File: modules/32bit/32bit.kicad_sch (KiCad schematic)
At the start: 53 parts, among them J5 USB_C_Receptacle_USB2.0_14P, SW1 K2-1808SN-A4SW-01, SW2 K2-1808SN-A4SW-01, SW4 K2-1808SN-A4SW-01, U1 ESP32-S3-WROOM-1U-N16R8, U3 MCP6002-xSN

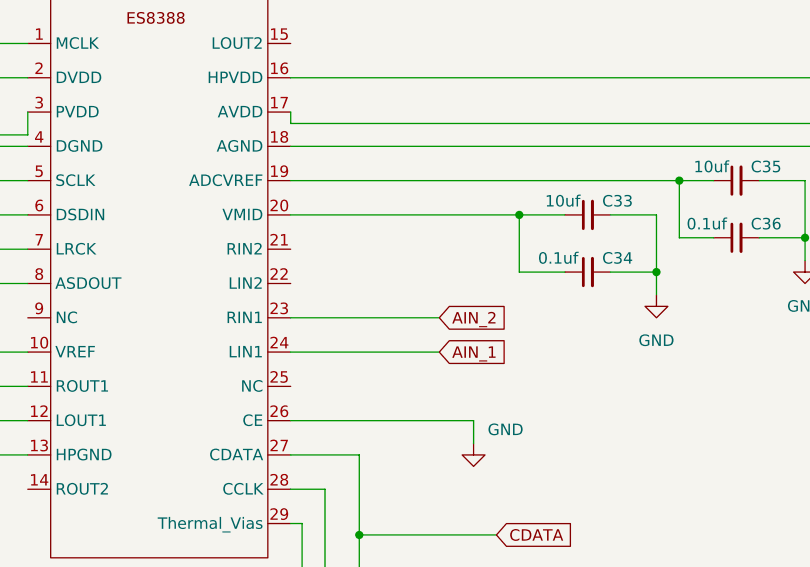
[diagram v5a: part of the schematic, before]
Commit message: Add better routing for power
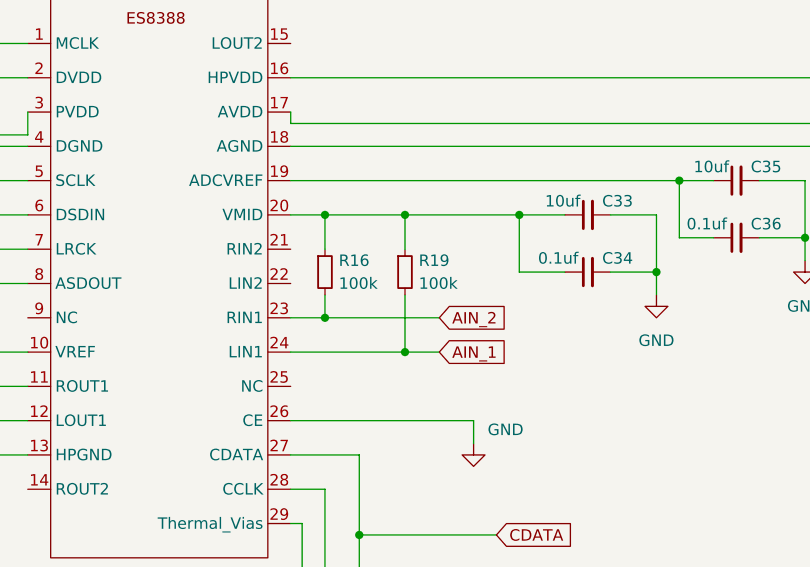
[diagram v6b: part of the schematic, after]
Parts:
- added R16, R19: 100k, Resistor_SMD:R_0402_1005Metric, symbol Device:R_Small
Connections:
- net AIN_1: now also R19.2
- net AIN_2: now also R16.2
- net at C33.1, C34.1, U4.20 (VMID): now also R16.1, R19.1
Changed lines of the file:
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@@
 	)
 	(junction
+		(at 139.7 210.82)
+		(diameter 0)
+		(color 0 0 0 0)
+	)
+	(junction
 		(at 509.27 38.1)
 		(diameter 0)
@@
 	)
 	(junction
+		(at 139.7 226.06)
+		(diameter 0)
+		(color 0 0 0 0)
+	)
+	(junction
 		(at 180.34 95.25)
 		(diameter 0)
@@
 	)
 	(junction
+		(at 130.81 210.82)
+		(diameter 0)
+		(color 0 0 0 0)
+	)
+	(junction
 		(at 45.72 83.82)
 		(diameter 0)
@@
 	)
 	(junction
+		(at 130.81 222.25)
+		(diameter 0)
+		(color 0 0 0 0)
+	)
+	(junction
 		(at 195.58 60.96)
 		(diameter 0)
@@
 	(wire
 		(pts
-			(xy 152.4 210.82) (xy 127 210.82)
+			(xy 152.4 210.82) (xy 139.7 210.82)
 		)
 		(stroke
@@
 	(wire
 		(pts
+			(xy 139.7 226.06) (xy 143.51 226.06)
+		)
+		(stroke
+			(width 0)
+			(type default)
+		)
+	)
+	(wire
+		(pts
 			(xy 45.72 233.68) (xy 53.34 233.68)
 		)
@@
 	(wire
 		(pts
-			(xy 127 222.25) (xy 143.51 222.25)
+			(xy 127 222.25) (xy 130.81 222.25)
 		)
 		(stroke
@@
 	(wire
 		(pts
+			(xy 130.81 222.25) (xy 143.51 222.25)
+		)
+		(stroke
+			(width 0)
+			(type default)
+		)
+	)
+	(wire
+		(pts
 			(xy 130.81 241.3) (xy 127 241.3)
 		)
@@
 	(wire
 		(pts
+			(xy 130.81 219.71) (xy 130.81 222.25)
+		)
+		(stroke
+			(width 0)
+			(type default)
+		)
+	)
+	(wire
+		(pts
 			(xy 127 195.58) (xy 248.92 195.58)
 		)
@@
 	(wire
 		(pts
+			(xy 130.81 210.82) (xy 130.81 214.63)
+		)
+		(stroke
+			(width 0)
+			(type default)
+		)
+	)
+	(wire
+		(pts
 			(xy 63.5 201.93) (xy 97.79 201.93)
 		)
@@
 	(wire
 		(pts
+			(xy 139.7 210.82) (xy 130.81 210.82)
+		)
+		(stroke
+			(width 0)
+			(type default)
+		)
+	)
+	(wire
+		(pts
 			(xy 127 203.2) (xy 203.2 203.2)
 		)
@@
 	(wire
 		(pts
+			(xy 139.7 210.82) (xy 139.7 214.63)
+		)
+		(stroke
+			(width 0)
+			(type default)
+		)
+	)
+	(wire
+		(pts
 			(xy 142.24 251.46) (xy 149.86 251.46)
 		)
@@
 	(wire
 		(pts
+			(xy 139.7 219.71) (xy 139.7 226.06)
+		)
+		(stroke
+			(width 0)
+			(type default)
+		)
+	)
+	(wire
+		(pts
 			(xy 30.48 107.95) (xy 30.48 110.49)
 		)
@@
 	(wire
 		(pts
-			(xy 127 226.06) (xy 143.51 226.06)
+			(xy 127 226.06) (xy 139.7 226.06)
 		)
 		(stroke
@@
 	(wire
 		(pts
+			(xy 130.81 210.82) (xy 127 210.82)
+		)
+		(stroke
+			(width 0)
+			(type default)
+		)
+	)
+	(wire
+		(pts
 			(xy 203.2 222.25) (xy 217.17 222.25)
 		)
@@
 					(unit 1)
 				)
+			)
+		)
+	)
+	(symbol
+		(lib_id "Device:R_Small")
+		(at 130.81 217.17 0)
+		(unit 1)
+		(exclude_from_sim no)
+		(in_bom yes)
+		(on_board yes)
+		(dnp no)
+		(property "Reference" "R16"
+			(at 132.334 215.9 0)
+			(effects
+				(font
+					(size 1.27 1.27)
+				)
+				(justify left)
+			)
+		)
+		(property "Value" "100k"
+			(at 132.334 218.44 0)
+			(effects
+				(font
+					(size 1.27 1.27)
+				)
+				(justify left)
+			)
+		)
+		(property "Footprint" "Resistor_SMD:R_0402_1005Metric"
+			(at 130.81 217.17 0)
+			(effects
+				(font
+					(size 1.27 1.27)
+				)
+				(hide yes)
+			)
+		)
+		(property "Datasheet" "~"
+			(at 130.81 217.17 0)
+			(effects
+				(font
+					(size 1.27 1.27)
+				)
+				(hide yes)
+			)
+		)
+		(property "Description" "Resistor, small symbol"
+			(at 130.81 217.17 0)
+			(effects
+				(font
+					(size 1.27 1.27)
+				)
+				(hide yes)
+			)
+		)
+		(pin "2"
+		)
+		(pin "1"
+		)
+		(instances
+			(project "32bit"
+				(path "/b63493d3-5f6d-47e3-845b-87e7090fc1ab"
+					(reference "R16")
+					(unit 1)
+				)
+			)
+		)
+	)
+	(symbol
+		(lib_id "Device:R_Small")
+		(at 139.7 217.17 0)
+		(unit 1)
+		(exclude_from_sim no)
+		(in_bom yes)
+		(on_board yes)
+		(dnp no)
+		(property "Reference" "R19"
+			(at 141.224 215.9 0)
+			(effects
+				(font
+					(size 1.27 1.27)
+				)
+				(justify left)
+			)
+		)
+		(property "Value" "100k"
+			(at 141.224 218.44 0)
+			(effects
+				(font
+					(size 1.27 1.27)
+				)
+				(justify left)
+			)
+		)
+		(property "Footprint" "Resistor_SMD:R_0402_1005Metric"
+			(at 139.7 217.17 0)
+			(effects
+				(font
+					(size 1.27 1.27)
+				)
+				(hide yes)
+			)
+		)
+		(property "Datasheet" "~"
+			(at 139.7 217.17 0)
+			(effects
+				(font
+					(size 1.27 1.27)
+				)
+				(hide yes)
+			)
+		)
+		(property "Description" "Resistor, small symbol"
+			(at 139.7 217.17 0)
+			(effects
+				(font
+					(size 1.27 1.27)
+				)
+				(hide yes)
+			)
+		)
+		(pin "2"
+		)
+		(pin "1"
+		)
+		(instances
+			(project "32bit"
+				(path "/b63493d3-5f6d-47e3-845b-87e7090fc1ab"
+					(reference "R19")
+					(unit 1)
+				)

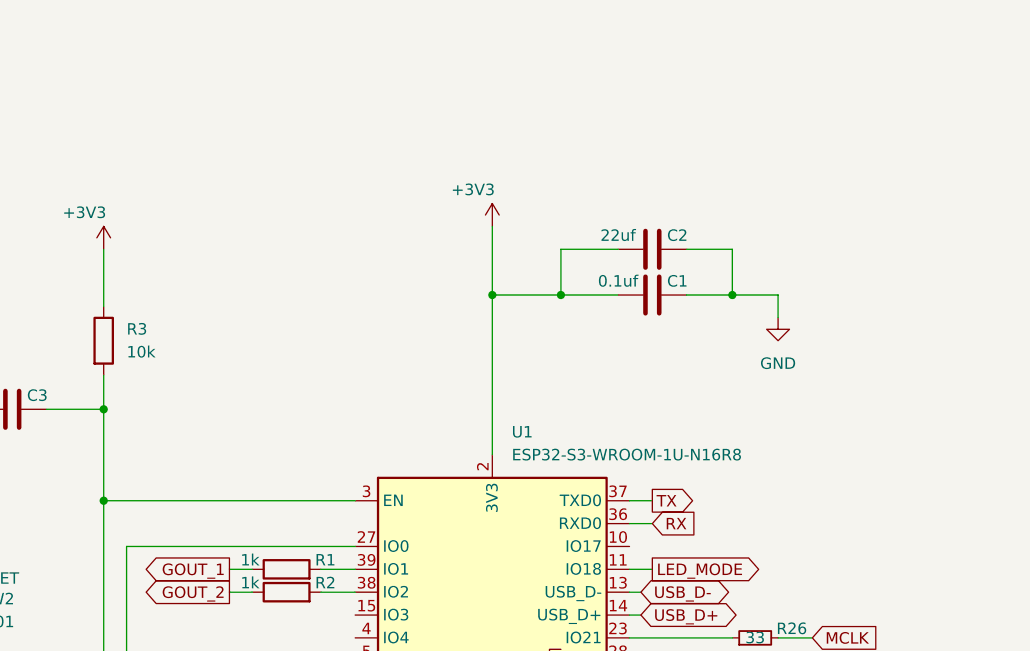
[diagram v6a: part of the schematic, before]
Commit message: Improve 32bit power supply
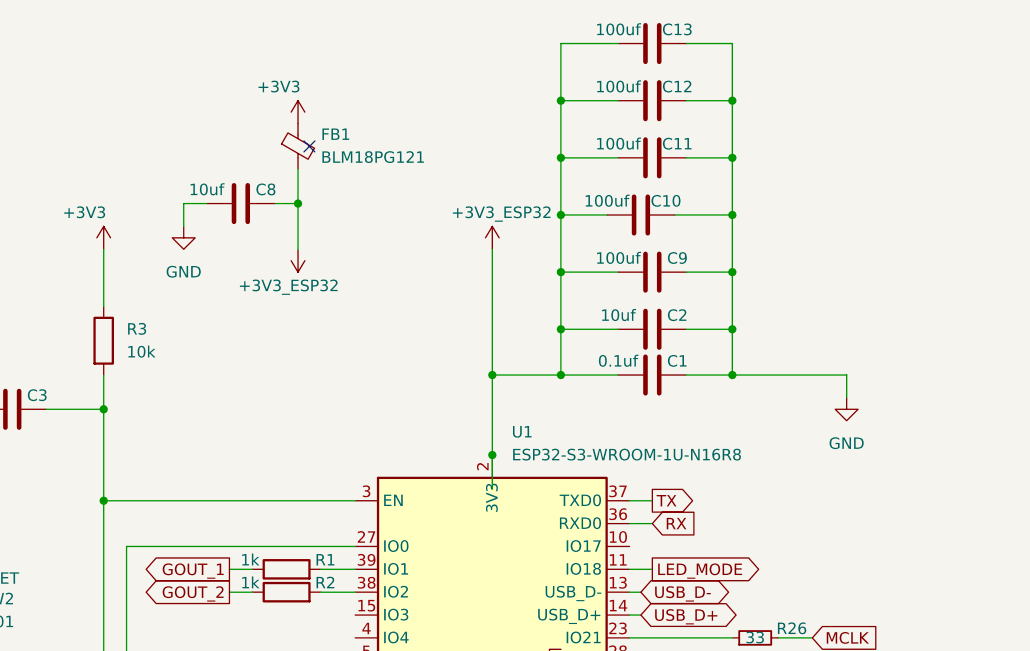
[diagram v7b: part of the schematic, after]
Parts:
- added C10, C11, C12, C13, C9: 100uf, Capacitor_SMD:C_1206_3216Metric, symbol Device:C
- added C8: 10uf, Capacitor_SMD:C_0603_1608Metric, symbol Device:C
- added FB1: BLM18PG121, Capacitor_SMD:C_0201_0603Metric, symbol Device:FerriteBead_Small
- C2: value 22uf -> 10uf
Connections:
- net +3V3: now also FB1.1; no longer C1.1, C2.1, U1.2 (3V3)
- net GND: now also C10.2, C11.2, C12.2, C13.2, C8.1, C9.2
- new net +3V3_ESP32: C1.1, C10.1, C11.1, C12.1, C13.1, C2.1, C8.2, C9.1, FB1.2, U1.2 (3V3)
- no-connect marks 0 -> 1
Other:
- moved on the sheet: C1, C2

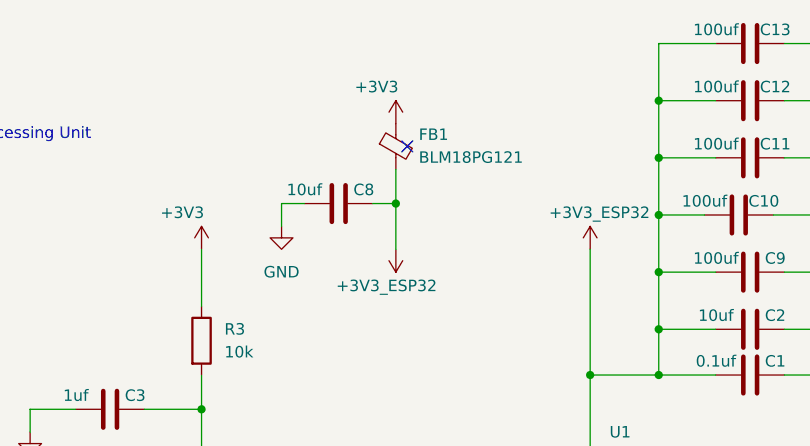
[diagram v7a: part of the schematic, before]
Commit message: 32bit: Use a known ferrite bead
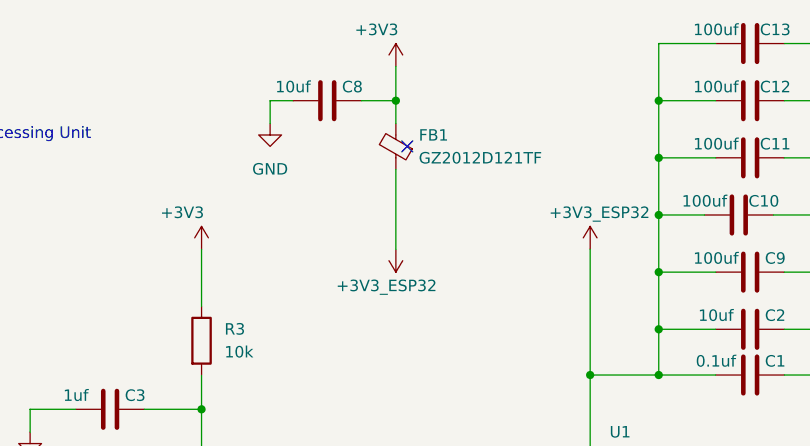
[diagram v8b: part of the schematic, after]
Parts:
- FB1: value BLM18PG121 -> GZ2012D121TF; footprint Capacitor_SMD:C_0201_0603Metric -> Capacitor_SMD:C_0805_2012Metric
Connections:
- net +3V3: now also C8.2, FB1.2; no longer FB1.1
- net +3V3_ESP32: now also FB1.1; no longer C8.2, FB1.2
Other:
- moved on the sheet: C8
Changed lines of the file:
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@@
 	)
 	(junction
-		(at 74.93 33.02)
-		(diameter 0)
-		(color 0 0 0 0)
-	)
-	(junction
 		(at 34.29 195.58)
 		(diameter 0)
@@
 	)
 	(junction
+		(at 74.93 21.59)
+		(diameter 0)
+		(color 0 0 0 0)
+	)
+	(junction
 		(at 224.79 54.61)
 		(diameter 0)
@@
 	(wire
 		(pts
-			(xy 64.77 33.02) (xy 62.23 33.02)
+			(xy 63.5 21.59) (xy 60.96 21.59)
 		)
 		(stroke
@@
 	(wire
 		(pts
+			(xy 71.12 21.59) (xy 74.93 21.59)
+		)
+		(stroke
+			(width 0)
+			(type default)
+		)
+	)
+	(wire
+		(pts
+			(xy 74.93 21.59) (xy 74.93 24.13)
+		)
+		(stroke
+			(width 0)
+			(type default)
+		)
+	)
+	(wire
+		(pts
 			(xy 96.52 38.1) (xy 96.52 52.07)
 		)
@@
 	(wire
 		(pts
+			(xy 74.93 17.78) (xy 74.93 21.59)
+		)
+		(stroke
+			(width 0)
+			(type default)
+		)
+	)
+	(wire
+		(pts
 			(xy 22.86 83.82) (xy 22.86 91.44)
 		)
@@
 	(wire
 		(pts
-			(xy 62.23 33.02) (xy 62.23 35.56)
+			(xy 60.96 21.59) (xy 60.96 24.13)
 		)
 		(stroke
@@
 	(wire
 		(pts
-			(xy 74.93 33.02) (xy 74.93 29.21)
+			(xy 74.93 29.21) (xy 74.93 38.1)
 		)
 		(stroke
@@
 	(wire
 		(pts
-			(xy 74.93 38.1) (xy 74.93 33.02)
-		)
-		(stroke
-			(width 0)
-			(type default)
-		)
-	)
-	(wire
-		(pts
 			(xy 130.81 251.46) (xy 130.81 241.3)
 		)
@@
 	(wire
 		(pts
-			(xy 72.39 33.02) (xy 74.93 33.02)
-		)
-		(stroke
-			(width 0)
-			(type default)
-		)
-	)
-	(wire
-		(pts
 			(xy 73.66 369.57) (xy 43.18 369.57)
 		)
@@
 	(symbol
 		(lib_id "Device:C")
-		(at 68.58 33.02 90)
+		(at 67.31 21.59 90)
 		(unit 1)
 		(exclude_from_sim no)
@@
 		(dnp no)
 		(property "Reference" "C8"
-			(at 71.374 31.496 90)
+			(at 70.104 20.066 90)
 			(effects
 				(font
@@
 		)
 		(property "Value" "10uf"
-			(at 64.77 31.496 90)
+			(at 63.5 20.066 90)
 			(effects
 				(font
@@
 		)
 		(property "Footprint" "Capacitor_SMD:C_0603_1608Metric"
-			(at 72.39 32.0548 0)
+			(at 71.12 20.6248 0)
 			(effects
 				(font
@@
 		)
 		(property "Datasheet" "~"
-			(at 68.58 33.02 0)
+			(at 67.31 21.59 0)
 			(effects
 				(font
@@
 		)
 		(property "Description" "Unpolarized capacitor"
-			(at 68.58 33.02 0)
+			(at 67.31 21.59 0)
 			(effects
 				(font
@@
 	)
 	(symbol
-		(lib_id "Device:FerriteBead_Small")
-		(at 74.93 26.67 0)
-		(unit 1)
-		(exclude_from_sim no)
-		(in_bom yes)
-		(on_board yes)
-		(dnp no)
-		(fields_autoplaced yes)
-		(property "Reference" "FB1"
-			(at 77.47 25.3618 0)
-			(effects
-				(font
-					(size 1.27 1.27)
-				)
-				(justify left)
-			)
-		)
-		(property "Value" "BLM18PG121"
-			(at 77.47 27.9018 0)
-			(effects
-				(font
-					(size 1.27 1.27)
-				)
-				(justify left)
-			)
-		)
-		(property "Footprint" "Capacitor_SMD:C_0201_0603Metric"
-			(at 73.152 26.67 90)
-			(effects
-				(font
-					(size 1.27 1.27)
-				)
-				(hide yes)
-			)
-		)
-		(property "Datasheet" "~"
-			(at 74.93 26.67 0)
-			(effects
-				(font
-					(size 1.27 1.27)
-				)
-				(hide yes)
-			)
-		)
-		(property "Description" "Ferrite bead, small symbol"
-			(at 74.93 26.67 0)
-			(effects
-				(font
-					(size 1.27 1.27)
-				)
-				(hide yes)
-			)
-		)
-		(pin "2"
-		)
-		(pin "1"
-		)
-		(instances
-			(project ""
-				(path "/b63493d3-5f6d-47e3-845b-87e7090fc1ab"
-					(reference "FB1")
-					(unit 1)
-				)
-			)
-		)
-	)
-	(symbol
 		(lib_id "power:GND")
 		(at 520.7 144.78 0)
@@
 	)
 	(symbol
+		(lib_id "Device:FerriteBead_Small")
+		(at 74.93 26.67 180)
+		(unit 1)
+		(exclude_from_sim yes)
+		(in_bom yes)
+		(on_board yes)
+		(dnp no)
+		(fields_autoplaced yes)
+		(property "Reference" "FB1"
+			(at 77.47 25.438 0)
+			(effects
+				(font
+					(size 1.27 1.27)
+				)
+				(justify right)
+			)
+		)
+		(property "Value" "GZ2012D121TF"
+			(at 77.47 27.978 0)
+			(effects
+				(font
+					(size 1.27 1.27)
+				)
+				(justify right)
+			)
+		)
+		(property "Footprint" "Capacitor_SMD:C_0805_2012Metric"
+			(at 76.708 26.67 90)
+			(effects
+				(font
+					(size 1.27 1.27)
+				)
+				(hide yes)
+			)
+		)
+		(property "Datasheet" "~"
+			(at 74.93 26.67 0)
+			(effects
+				(font
+					(size 1.27 1.27)
+				)
+				(hide yes)
+			)
+		)
+		(property "Description" "Ferrite bead, small symbol"
+			(at 74.93 26.67 0)
+			(effects
+				(font
+					(size 1.27 1.27)
+				)
+				(hide yes)
+			)
+		)
+		(pin "1"
+		)
+		(pin "2"
+		)
+		(instances
+			(project "32bit"
+				(path "/b63493d3-5f6d-47e3-845b-87e7090fc1ab"
+					(reference "FB1")
+					(unit 1)
+				)
+			)
+		)
+	)
+	(symbol
 		(lib_id "Device:C")
 		(at 114.3 27.94 90)
@@
 	(symbol
 		(lib_id "power:+5V")
-		(at 74.93 24.13 0)
+		(at 74.93 17.78 0)
 		(unit 1)
 		(exclude_from_sim no)
@@
 		(dnp no)
 		(property "Reference" "#PWR09"
-			(at 74.93 27.94 0)
+			(at 74.93 21.59 0)
 			(effects
 				(font
@@
 		)
 		(property "Value" "+3V3"
-			(at 70.358 20.066 0)
+			(at 70.358 13.716 0)
 			(effects
 				(font
@@
 		)
 		(property "Footprint" ""
-			(at 74.93 24.13 0)
+			(at 74.93 17.78 0)
 			(effects
 				(font
@@
 		)
 		(property "Datasheet" ""
-			(at 74.93 24.13 0)
+			(at 74.93 17.78 0)
 			(effects
 				(font
@@
 		)
 		(property "Description" "Power symbol creates a global label with name \"+5V\""
-			(at 74.93 24.13 0)
+			(at 74.93 17.78 0)
 			(effects
 				(font
@@
 	(symbol
 		(lib_id "power:GND")
-		(at 62.23 35.56 0)
+		(at 60.96 24.13 0)
 		(unit 1)
 		(exclude_from_sim no)
@@
 		(dnp no)
 		(property "Reference" "#PWR021"
-			(at 62.23 41.91 0)
+			(at 60.96 30.48 0)
 			(effects
 				(font
@@
 		)
 		(property "Value" "GND"
-			(at 62.23 40.64 0)
+			(at 60.96 29.21 0)
 			(effects
 				(font
@@
 		)
 		(property "Footprint" ""
-			(at 62.23 35.56 0)
+			(at 60.96 24.13 0)
 			(effects
 				(font
@@
 		)
 		(property "Datasheet" ""
-			(at 62.23 35.56 0)
+			(at 60.96 24.13 0)
 			(effects
 				(font
@@
 		)
 		(property "Description" "Power symbol creates a global label with name \"GND\" , ground"
-			(at 62.23 35.56 0)
+			(at 60.96 24.13 0)
 			(effects
 				(font
